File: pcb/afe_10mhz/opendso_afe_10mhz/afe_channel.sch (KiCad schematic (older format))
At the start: 94 parts, among them IC10 L9110, IC11 DG4052EEN, IC12 L9110, IC13 VO1400AEFTR, IC14 AD8132ARZ, IC15 VO1400AEFTR, IC16 AD8065ART-R2, IC17 MCP6H01T-E

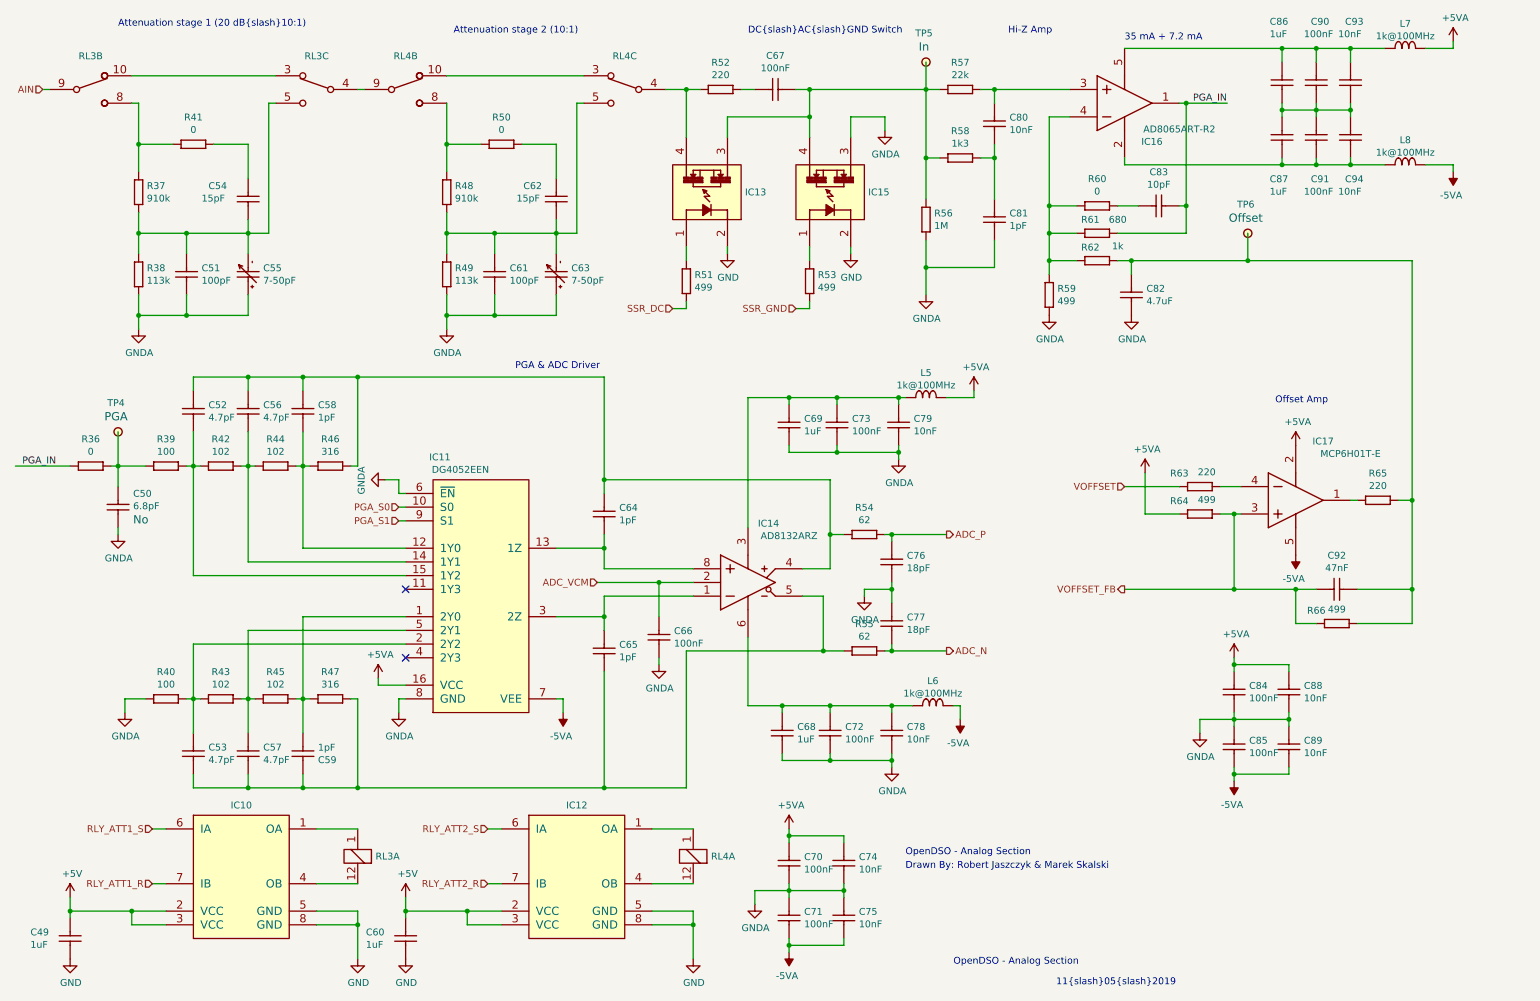
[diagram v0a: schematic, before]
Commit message: AFE schematic: finished port to KiCad
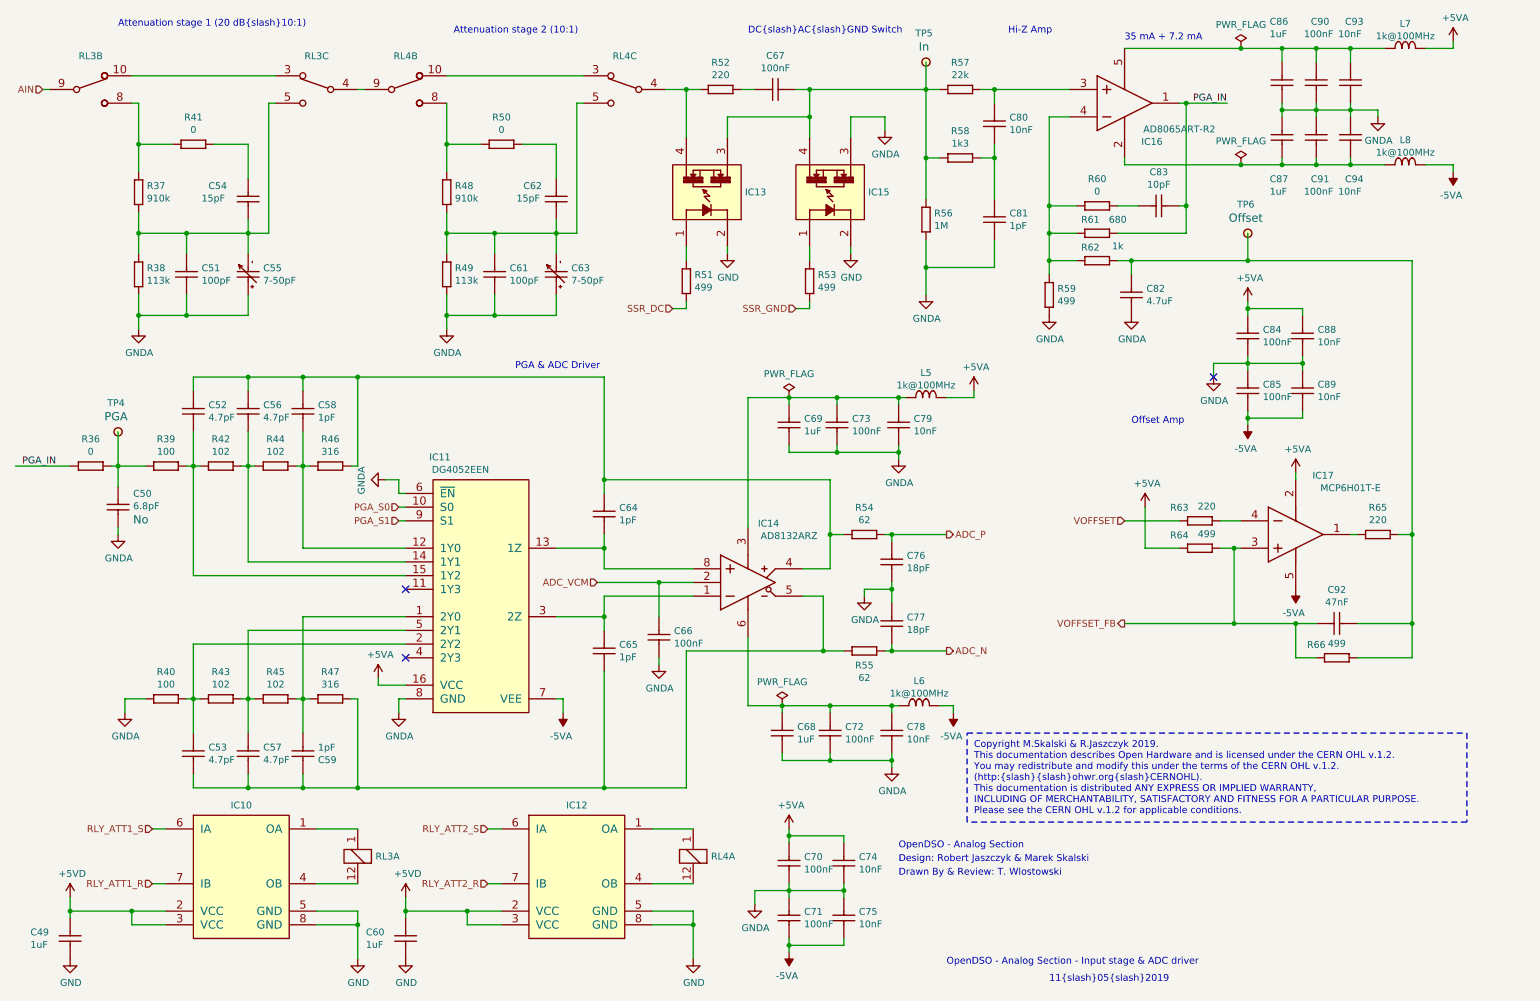
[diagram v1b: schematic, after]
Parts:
- removed C67: CPER_100NF_100V_10%_500-250X720X650, CAPR500-250X720X650, symbol Capacitors_THD:CPER_100NF_100V_10%_500-250X720X650
- added C67: CC1206_100NF_100V_10%_X7R, Capacitors SMD:CAPC3216X140N, symbol Capacitors_SMD:CC1206_100NF_100V_10%_X7R
- C49, C50, C54, C58, C59, C60, C62, C64, C65, C66, C68, C69, C70, C71, C72, C73, C74, C75, C76, C77, C78, C79, C80, C81, C83, C84, C85, C86, C87, C88, C89, C90, C91, C93, C94: footprint CAPC1608X87N -> Capacitors SMD:CAPC1608X87N
- C51, C61: footprint CAPC1608X90N -> Capacitors SMD:CAPC1608X90N
- C55, C63: footprint CAPV_MURATA_TZB4_TYPE A -> Capacitors SMD:CAPV_MURATA_TZB4_TYPE A
- C82: footprint CAPC2012X135N -> Capacitors SMD:CAPC2012X135N
- IC14: footprint SOIC127P600X175-8N -> ICs And Semiconductors SMD:SOIC127P600X175-8N
- IC16: footprint SOT95P280X145-5N -> ICs And Semiconductors SMD:SOT95P280X145-5N
- R36, R37, R38, R41, R48, R49, R50, R51, R52, R53, R56, R57, R58, R59, R60, R62, R63, R64, R65, R66: footprint RESC1608X55N -> Resistors SMD:RESC1608X55N
- R61: footprint RESC1608X64N -> Resistors SMD:RESC1608X64N
- RL3, RL4: footprint Relays:REL_OMRON_G6SU-2F -> Relay_SMD:Relay_DPDT_Omron_G6SU-2F
- TP4, TP5, TP6: footprint TPS127 -> Pads:TPS127
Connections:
- net GNDA: now also C86.1, C87.2, C90.1, C91.2, C93.1, C94.2
- net at IC13.3 (C), IC15.4 (E), R56.2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: now also C67.2
- net at R52.2: now also C67.1
- net +5V renamed +5VD
- no-connect marks 2 -> 3
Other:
- note added: "Copyright M.Skalski & R.Jaszczyk 2019.\nThis documentation describes Open Hardware and is licensed under the CERN OHL v.1.2.\nYou may redistribute and modify this under the terms of the CERN OHL v.1.2.\n(http://ohwr.org/CERNOHL).\nThis documentation is distributed ANY EXPRESS OR IMPLIED WARRANTY,\nINCLUDING OF MERCHANTABILITY, SATISFACTORY AND FITNESS FOR A PARTICULAR PURPOSE.\n…"
- note added: "Design: Robert Jaszczyk & Marek Skalski\n"
- note added: "Drawn By & Review: T. Wlostowski\n"
- note added: "OpenDSO - Analog Section - Input stage & ADC driver"
- note removed: "Drawn By: Robert Jaszczyk & Marek Skalski\n"
- moved on the sheet: C84, C85, C88, C89, C92, IC17, L6, R63, R64, R65, R66
